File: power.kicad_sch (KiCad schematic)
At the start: 127 parts, among them Q2 BC817-25W, Q3 DZDH0401DW, Q4 DZDH0401DW, Q5 SI7613DN-T1-GE3, Q6 SI7613DN-T1-GE3, U1 LT8350RV#PBF, U2 MP2386GG, U3 TPS65983BAZBHR

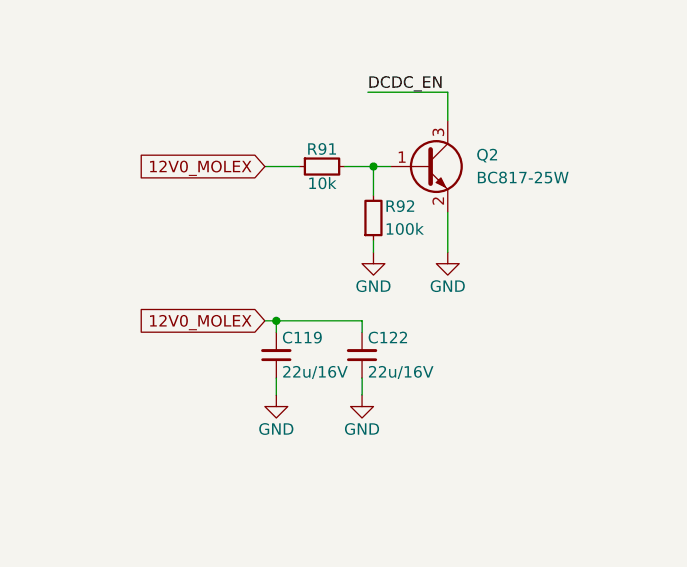
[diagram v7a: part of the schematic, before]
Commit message: Add TP for 12V_EXT, move L1 and L2 to improve access to U1 and U2 pads, update revision
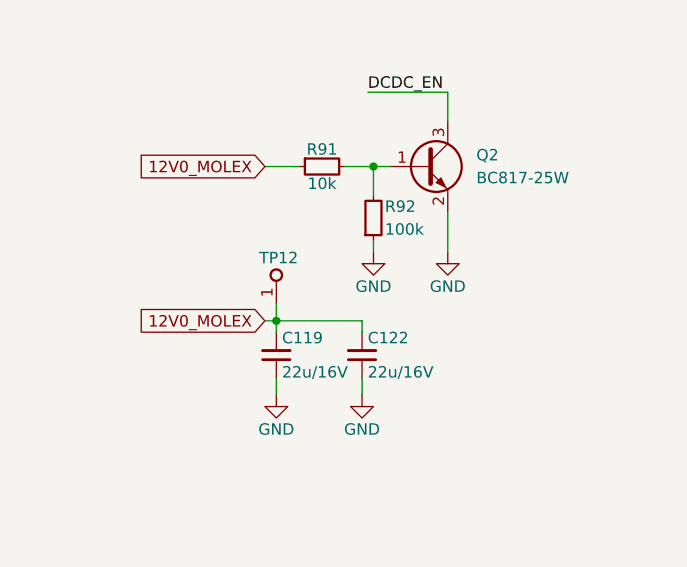
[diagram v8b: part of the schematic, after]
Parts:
- added TP12: TP_1mm_SMD, antmicro-footprints:TP_SMD_1mm, symbol antmicroTestPoints:TP_1mm_SMD
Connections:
- net 12V0_MOLEX: now also TP12.1
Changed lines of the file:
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@@
+    (stroke (width 0) (type default) (color 0 0 0 0))
+  )
+  (wire (pts (xy 46.355 257.81) (xy 46.355 259.715))
     (stroke (width 0) (type default) (color 0 0 0 0))
   )
@@
     )
     (pin "1")
+  )
+  (symbol (lib_id "antmicroTestPoints:TP_1mm_SMD") (at 46.355 257.81 90) (unit 1)
+    (in_bom yes) (on_board yes)
+    (property "Reference" "TP12" (id 0) (at 44.45 252.73 90)
+      (effects (font (size 1.27 1.27) (thickness 0.15)) (justify right))
+    )
+    (property "Value" "TP_1mm_SMD" (id 1) (at 48.26 254.6349 90)
+      (effects (font (size 1.27 1.27) (thickness 0.15)) (justify right) hide)
+    )
+    (property "Footprint" "antmicro-footprints:TP_SMD_1mm" (id 2) (at 56.515 242.57 0)
+      (effects (font (size 1.27 1.27) (thickness 0.15)) (justify left bottom) hide)
+    )
+    (property "Datasheet" "" (id 3) (at 59.055 242.57 0)
+      (effects (font (size 1.27 1.27) (thickness 0.15)) (justify left bottom) hide)
+    )
+    (property "Copyright" "Copyright (c) 2023 Antmicro" (id 4) (at 61.595 242.57 0)
+      (effects (font (size 1.27 1.27) (thickness 0.15)) (justify left bottom) hide)
+    )
+    (property "License" "Apache-2.0 License" (id 5) (at 64.135 242.57 0)
+      (effects (font (size 1.27 1.27) (thickness 0.15)) (justify left bottom) hide)
+    )
+    (property "Manufacturer" "None" (id 6) (at 48.26 257.1749 90)
+      (effects (font (size 1.27 1.27)) (justify right) hide)
+    )
+    (pin "1")
